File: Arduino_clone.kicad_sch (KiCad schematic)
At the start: 10 parts

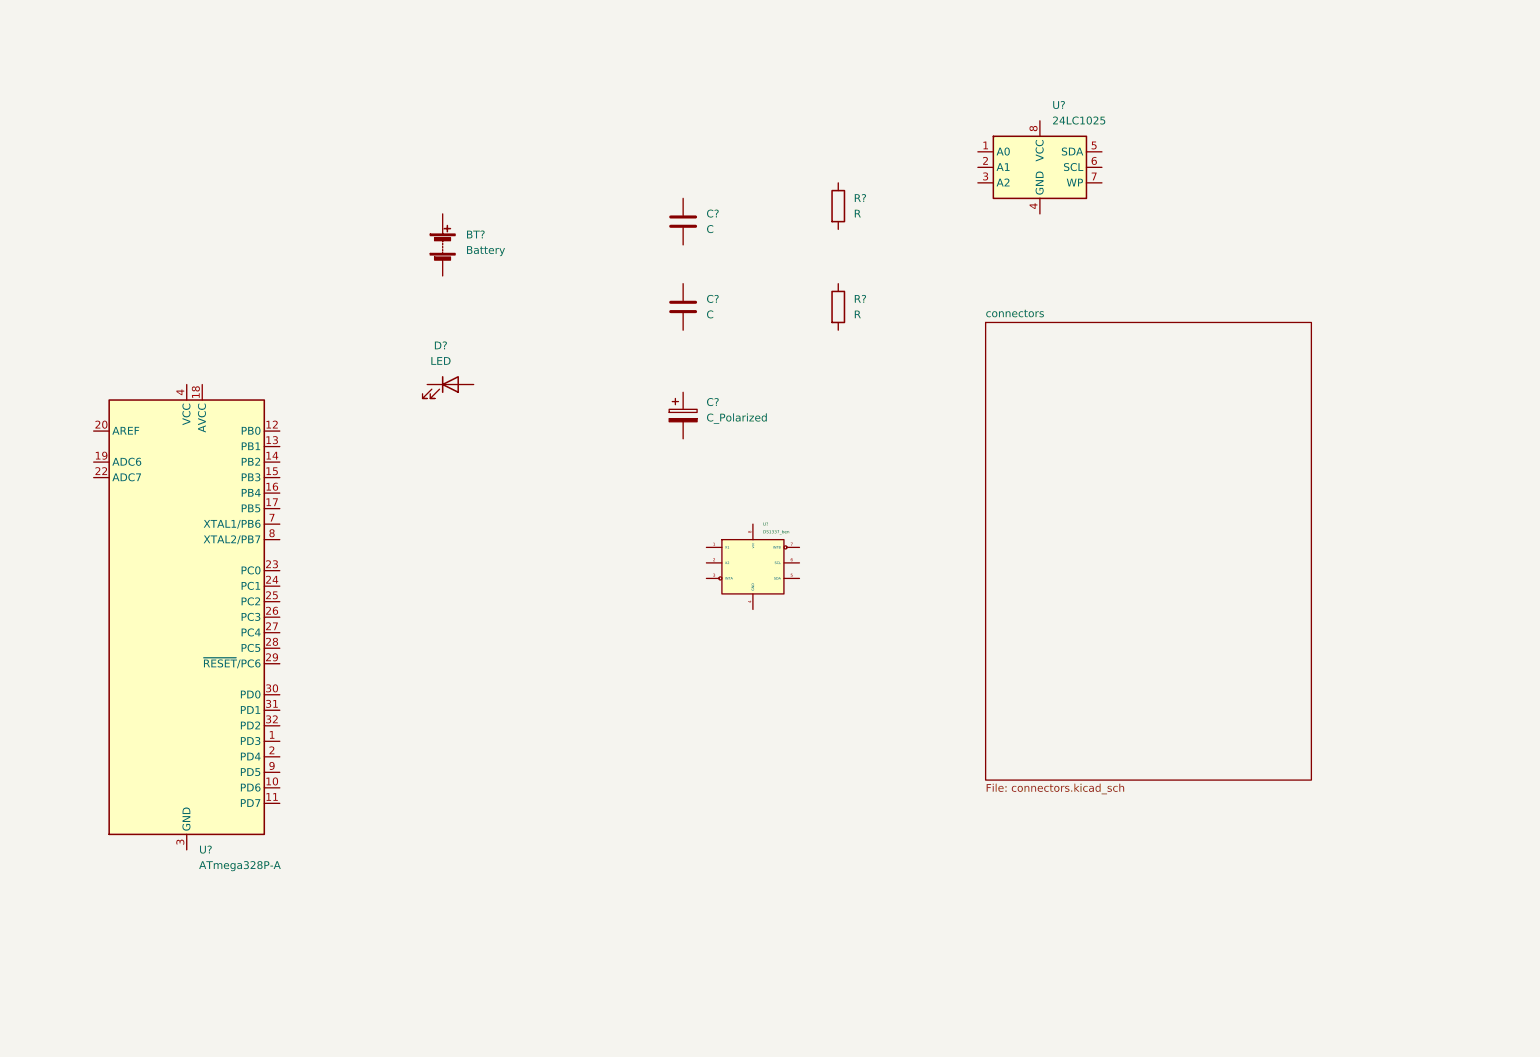
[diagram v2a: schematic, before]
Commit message: annotate symbol
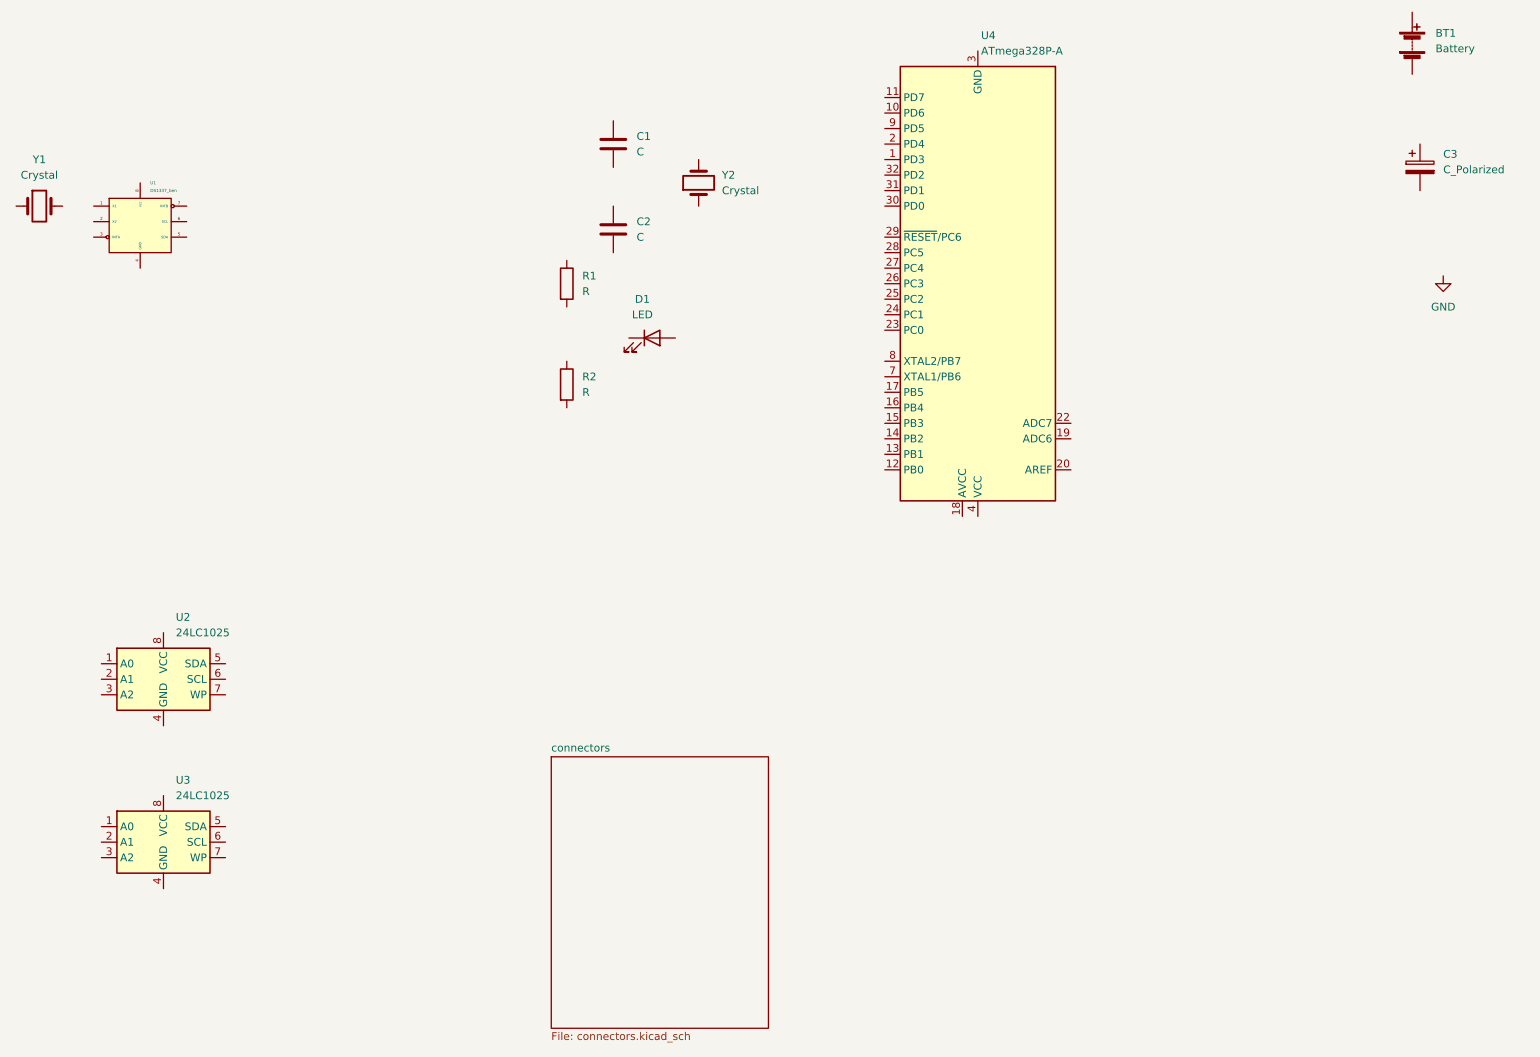
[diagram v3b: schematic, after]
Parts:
- added U3: 24LC1025, symbol Memory_EEPROM:24LC1025
- added Y1, Y2: Crystal, symbol Device:Crystal
- gave numbers to parts that had none: 10
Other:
- moved on the sheet: BT1, C1, C2, C3, D1, R1, R2, U1, U2, U4
